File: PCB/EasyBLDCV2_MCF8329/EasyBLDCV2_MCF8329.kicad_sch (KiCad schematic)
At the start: 0 parts

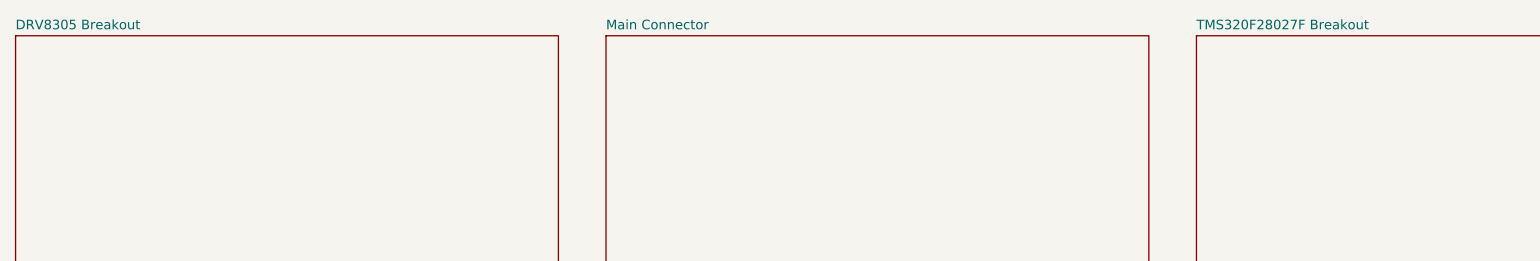
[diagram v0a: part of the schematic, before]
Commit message: Deleted V1 Relics, redid power stage
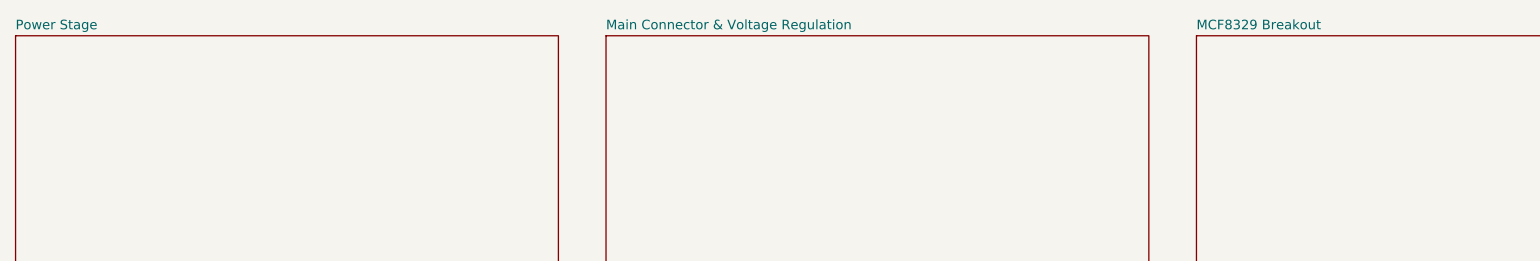
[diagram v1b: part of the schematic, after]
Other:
- sheet DRV8305 Breakout renamed Power Stage
- sheet Main Connector renamed Main Connector & Voltage Regulation
- sheet TMS320F28027F Breakout renamed MCF8329 Breakout
- title: Easy ESC -> Easy BLDC
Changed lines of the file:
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@@
 	(paper "A4")
 	(title_block
-		(title "Easy ESC")
+		(title "Easy BLDC")
 		(date "2024-08-06")
-		(rev "1.0")
+		(rev "2.0")
 		(company "Peter Buckley Engineering")
 	)
@@
 			(color 0 0 0 0.0000)
 		)
-		(property "Sheetname" "Main Connector"
+		(property "Sheetname" "Main Connector & Voltage Regulation"
 			(at 113.03 61.5184 0)
 			(effects
@@
 		)
 		(instances
-			(project "EasyBLDCV1_DRV8305"
+			(project "EasyBLDCV2_MCF8329"
 				(path "/6c304649-7c80-4a4c-b925-07b9210ad53d"
 					(page "1")
@@
 			(color 0 0 0 0.0000)
 		)
-		(property "Sheetname" "TMS320F28027F Breakout"
+		(property "Sheetname" "MCF8329 Breakout"
 			(at 191.77 61.5184 0)
 			(effects
@@
 		)
 		(instances
-			(project "EasyBLDCV1_DRV8305"
+			(project "EasyBLDCV2_MCF8329"
 				(path "/6c304649-7c80-4a4c-b925-07b9210ad53d"
 					(page "3")
@@
 			(color 0 0 0 0.0000)
 		)
-		(property "Sheetname" "DRV8305 Breakout"
+		(property "Sheetname" "Power Stage"
 			(at 34.29 61.5184 0)
 			(effects
@@
 		)
 		(instances
-			(project "EasyBLDCV1_DRV8305"
+			(project "EasyBLDCV2_MCF8329"
 				(path "/6c304649-7c80-4a4c-b925-07b9210ad53d"
 					(page "2")

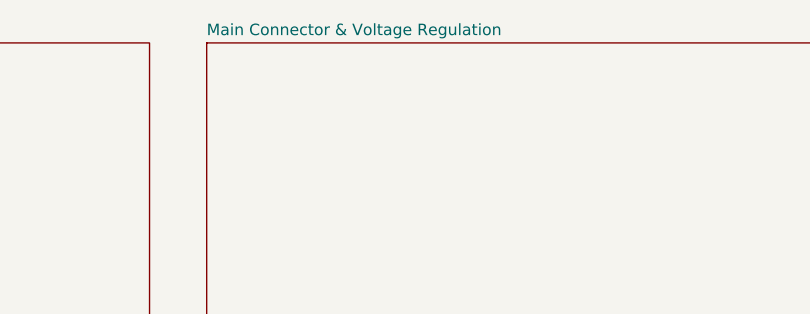
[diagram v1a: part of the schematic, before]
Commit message: Added  comments to schematic
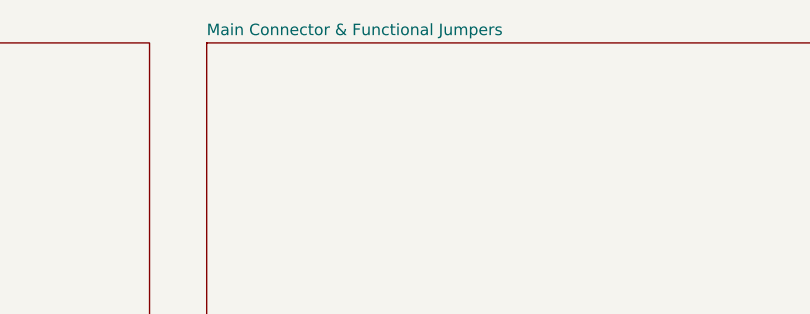
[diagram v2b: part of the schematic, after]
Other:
- sheet Main Connector & Voltage Regulation renamed Main Connector & Functional Jumpers
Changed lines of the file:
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@@
 			(color 0 0 0 0.0000)
 		)
-		(property "Sheetname" "Main Connector & Voltage Regulation"
+		(property "Sheetname" "Main Connector & Functional Jumpers"
 			(at 113.03 61.5184 0)
 			(effects

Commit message: Finished schematic
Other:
- sheet Main Connector & Functional Jumpers renamed Main Connector & Debug
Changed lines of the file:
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@@
 			(color 0 0 0 0.0000)
 		)
-		(property "Sheetname" "Main Connector & Functional Jumpers"
+		(property "Sheetname" "Main Connector & Debug"
 			(at 113.03 61.5184 0)
 			(effects
